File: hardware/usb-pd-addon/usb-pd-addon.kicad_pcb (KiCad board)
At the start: 2 copper layers, 48 x 40 mm, 73 parts, among them J1 Conn_02x10_Odd_Even, J2 Conn_02x10_Odd_Even, J3 USB_TYPE_C, J4 Conn_02x05_Odd_Even, J5 Conn_02x05_Odd_Even, J6 TPAS, J7 TPBS, U1 FUSB302B, U2 AP2171W, U3 SN74AVC1T45DBVR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

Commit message: Updated README, better silk for voltage control jumpers.
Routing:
- net GND: vias 25 -> 28
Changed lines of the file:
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@@
   (general
     (thickness 1.6)
-    (drawings 98)
-    (tracks 589)
+    (drawings 109)
+    (tracks 590)
     (zones 0)
     (modules 73)
@@
     )
   )
+  (gr_poly (pts (xy 56.5785 51.4985) (xy 55.1815 51.4985) (xy 55.1815 50.1015) (xy 56.5785 50.1015)) (layer B.Mask) (width 0.1))
+  (gr_line (start 59.69 36.068) (end 59.69 36.703) (layer F.SilkS) (width 0.12))
+  (gr_line (start 62.23 36.068) (end 62.23 36.703) (layer F.SilkS) (width 0.12))
+  (gr_line (start 64.77 36.068) (end 64.77 36.703) (layer F.SilkS) (width 0.12))
+  (gr_line (start 67.31 36.068) (end 67.31 36.703) (layer F.SilkS) (width 0.12))
+  (gr_line (start 69.85 36.068) (end 69.85 36.703) (layer F.SilkS) (width 0.12))
+  (gr_line (start 52.07 36.068) (end 52.07 36.703) (layer F.SilkS) (width 0.12))
+  (gr_line (start 49.53 36.068) (end 49.53 36.703) (layer F.SilkS) (width 0.12))
+  (gr_line (start 46.99 36.068) (end 46.99 36.703) (layer F.SilkS) (width 0.12))
+  (gr_line (start 44.45 36.068) (end 44.45 36.703) (layer F.SilkS) (width 0.12))
+  (gr_line (start 41.91 36.068) (end 41.91 36.703) (layer F.SilkS) (width 0.12))
   (gr_text 3V3 (at 34.036 66.802 270) (layer F.SilkS)
     (effects (font (size 1 1) (thickness 0.15)))
@@
   (segment (start 76.2 55.88) (end 76.2 58.42) (width 0.3) (layer F.Cu) (net 1) (status 30))
   (segment (start 76.2 58.42) (end 76.2 60.96) (width 0.3) (layer F.Cu) (net 1) (status 30))
-  (via (at 55.88 50.8) (size 0.5) (drill 0.3) (layers F.Cu B.Cu) (net 1) (status 30))
+  (via (at 55.499 50.419) (size 0.5) (drill 0.3) (layers F.Cu B.Cu) (net 1) (status 30))
   (segment (start 59.1312 62.992) (end 59.13 63.552) (width 0.3) (layer F.Cu) (net 1))
   (segment (start 59.13 63.552) (end 59.13 64.535) (width 0.3) (layer F.Cu) (net 1) (status 20))
@@
   (via (at 36.576 66.04) (size 0.5) (drill 0.3) (layers F.Cu B.Cu) (net 1))
   (segment (start 35.56 66.0145) (end 36.5505 66.0145) (width 0.3) (layer F.Cu) (net 1))
+  (via (at 55.499 51.181) (size 0.5) (drill 0.3) (layers F.Cu B.Cu) (net 1) (status 30))
+  (via (at 56.261 51.181) (size 0.5) (drill 0.3) (layers F.Cu B.Cu) (net 1) (status 30))
+  (via (at 56.261 50.419) (size 0.5) (drill 0.3) (layers F.Cu B.Cu) (net 1) (status 30))
   (segment (start 36.83 39.37) (end 38.1 38.1) (width 0.2) (layer F.Cu) (net 4))
   (segment (start 36.83 62.23) (end 36.83 39.37) (width 0.2) (layer F.Cu) (net 4))
@@
   (segment (start 57.1425 52.0625) (end 57.1425 51.3) (width 0.2) (layer F.Cu) (net 7) (status 20))
   (segment (start 56.63 52.0625) (end 57.1425 52.0625) (width 0.2) (layer F.Cu) (net 7) (status 10))
-  (segment (start 57.63 59.535) (end 57.1425 59.0475) (width 0.2) (layer F.Cu) (net 7))
-  (segment (start 57.63 64.535) (end 57.63 59.535) (width 0.2) (layer F.Cu) (net 7) (status 10))
-  (segment (start 57.1425 59.0475) (end 57.1425 53.3475) (width 0.2) (layer F.Cu) (net 7))
   (segment (start 57.1425 53.3475) (end 57.1425 52.0625) (width 0.2) (layer F.Cu) (net 7))
   (segment (start 57.1425 53.3475) (end 57.1425 52.888) (width 0.2) (layer F.Cu) (net 7))
-  (via (at 57.1425 52.888) (size 0.5) (drill 0.3) (layers F.Cu B.Cu) (net 7))
+  (via (at 57.15 60.452) (size 0.5) (drill 0.3) (layers F.Cu B.Cu) (net 7))
+  (segment (start 57.1425 60.8255) (end 57.1425 53.3475) (width 0.2) (layer F.Cu) (net 7))
+  (segment (start 57.63 61.313) (end 57.1425 60.8255) (width 0.2) (layer F.Cu) (net 7))
+  (segment (start 57.63 64.535) (end 57.63 61.313) (width 0.2) (layer F.Cu) (net 7))
   (segment (start 55.118 52.0745) (end 55.13 52.0625) (width 0.2) (layer F.Cu) (net 8) (status 30))
   (segment (start 54.63 64.535) (end 54.58001 64.48501) (width 0.2) (layer F.Cu) (net 8) (status 30))
   (segment (start 54.6175 52.0625) (end 54.6175 51.3) (width 0.2) (layer F.Cu) (net 8) (status 20))
   (segment (start 55.13 52.0625) (end 54.6175 52.0625) (width 0.2) (layer F.Cu) (net 8) (status 10))
-  (segment (start 54.631129 59.085873) (end 54.631129 58.262127) (width 0.2) (layer F.Cu) (net 8))
-  (segment (start 54.525999 59.191003) (end 54.631129 59.085873) (width 0.2) (layer F.Cu) (net 8))
-  (segment (start 54.525999 63.256001) (end 54.525999 59.191003) (width 0.2) (layer F.Cu) (net 8))
-  (segment (start 54.63 63.360002) (end 54.525999 63.256001) (width 0.2) (layer F.Cu) (net 8))
-  (segment (start 54.63 64.535) (end 54.63 63.360002) (width 0.2) (layer F.Cu) (net 8) (status 10))
-  (segment (start 54.631129 58.262127) (end 54.618892 52.696108) (width 0.2) (layer F.Cu) (net 8))
   (segment (start 54.618892 52.696108) (end 54.6175 52.0625) (width 0.2) (layer F.Cu) (net 8))
   (segment (start 54.618892 52.886608) (end 54.618892 52.696108) (width 0.2) (layer F.Cu) (net 8))
-  (via (at 54.618892 52.886608) (size 0.5) (drill 0.3) (layers F.Cu B.Cu) (net 8))
+  (via (at 54.61 60.452) (size 0.5) (drill 0.3) (layers F.Cu B.Cu) (net 8))
+  (segment (start 54.525999 63.256001) (end 54.525999 60.939499) (width 0.2) (layer F.Cu) (net 8))
+  (segment (start 54.618892 60.846606) (end 54.618892 52.696108) (width 0.2) (layer F.Cu) (net 8))
+  (segment (start 54.525999 60.939499) (end 54.618892 60.846606) (width 0.2) (layer F.Cu) (net 8))
+  (segment (start 54.63 63.360002) (end 54.525999 63.256001) (width 0.2) (layer F.Cu) (net 8))
+  (segment (start 54.63 64.535) (end 54.63 63.360002) (width 0.2) (layer F.Cu) (net 8))
   (segment (start 55.13 49.5375) (end 55.13 49.034) (width 0.2) (layer F.Cu) (net 9) (status 10))
   (via (at 54.864 48.768) (size 0.5) (drill 0.3) (layers F.Cu B.Cu) (net 9))
@@
   (segment (start 57.1425 49.7915) (end 57.404 49.53) (width 0.2) (layer F.Cu) (net 14))
   (segment (start 57.1425 50.3) (end 57.1425 49.7915) (width 0.2) (layer F.Cu) (net 14) (status 10))
-  (segment (start 55.8725 51.6965) (end 55.8725 53.3475) (width 0.3) (layer B.Cu) (net 14))
-  (segment (start 57.404 50.165) (end 55.8725 51.6965) (width 0.3) (layer B.Cu) (net 14))
-  (segment (start 57.404 49.53) (end 57.404 50.165) (width 0.3) (layer B.Cu) (net 14))
   (segment (start 64.4525 59.69) (end 62.865 58.1025) (width 0.3) (layer B.Cu) (net 14))
   (segment (start 66.294 59.69) (end 64.4525 59.69) (width 0.3) (layer B.Cu) (net 14))
@@
   (segment (start 69.85 62.23) (end 72.644 65.024) (width 0.3) (layer B.Cu) (net 14))
   (segment (start 66.294 62.23) (end 69.85 62.23) (width 0.3) (layer B.Cu) (net 14))
+  (segment (start 57.404 51.816) (end 55.8725 53.3475) (width 0.3) (layer B.Cu) (net 14))
+  (segment (start 57.404 49.53) (end 57.404 51.816) (width 0.3) (layer B.Cu) (net 14))
   (segment (start 46.0375 48.895) (end 45.085 49.8475) (width 0.3) (layer B.Cu) (net 15))
   (segment (start 52.705 48.895) (end 46.0375 48.895) (width 0.3) (layer B.Cu) (net 15))

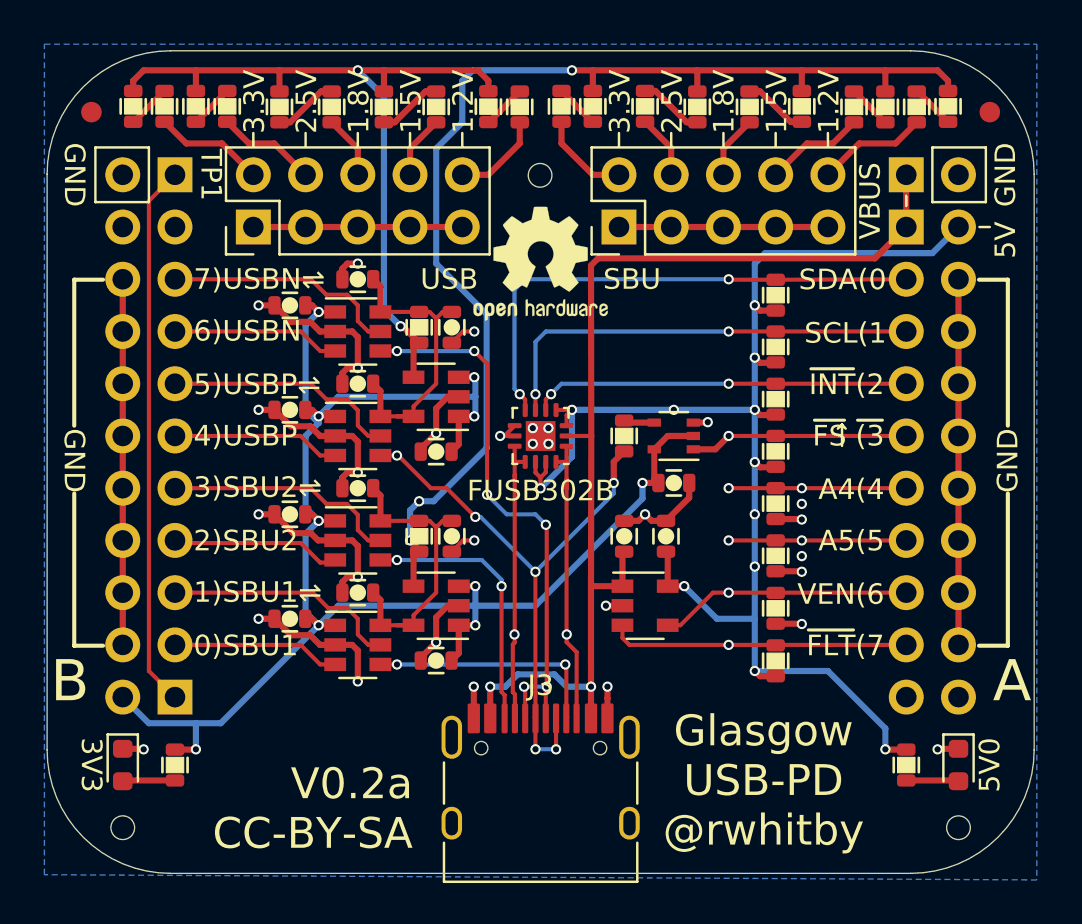
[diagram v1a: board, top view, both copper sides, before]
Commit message: Remove the D+ pullup, cause Glasgow will not support Luna USB stack.  Added 2 spare SOT23 footprints.
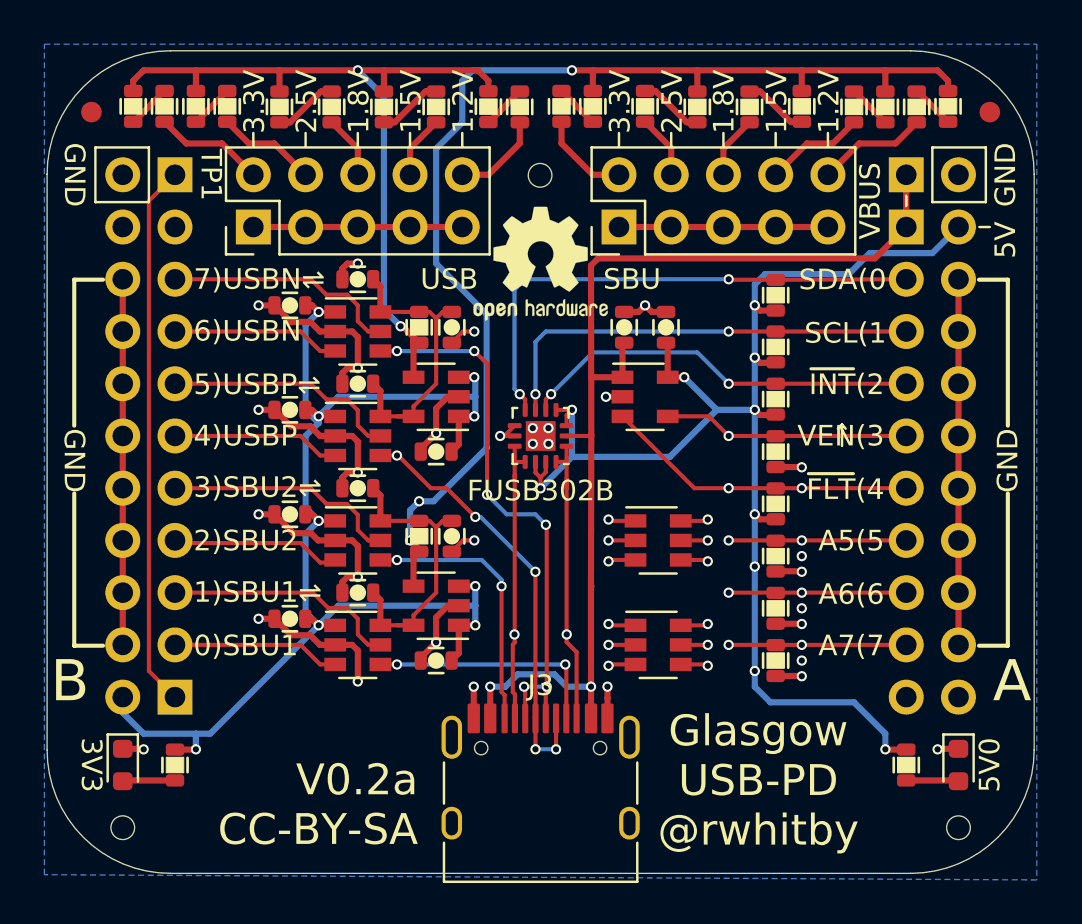
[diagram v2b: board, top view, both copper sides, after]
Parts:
- removed C15: 0.1u, pkl_dipol:C_0603
- removed R31: 1K5, pkl_dipol:R_0603
- removed U9: NC7SZ125P5X, Package_TO_SOT_SMD:SOT-353_SC-70-5
- added J8: Conn_02x03_Odd_Even, Package_TO_SOT_SMD:SOT-23-6, F.Cu at (61.6, 55.9)
- added J9: Conn_02x03_Odd_Even, Package_TO_SOT_SMD:SOT-23-6, F.Cu at (61.6, 61.0)
- moved C13 10.2 mm to (62.0, 45.5)
- moved C14 10.2 mm to (59.9, 45.5)
- moved U2 10.2 mm to (61.0, 48.9)
- moved R8 7.63 mm to (67.3, 54.1)
- moved R7 7.62 mm to (67.3, 51.6)
- moved R4 5.09 mm to (67.3, 56.6)
- moved R5 5.09 mm to (67.3, 59.2)
- moved R6 5.09 mm to (67.3, 61.7)
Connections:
- J2 pad 11: /A4 -> /~FLT
- J2 pad 15: /VEN -> /A6
- J2 pad 17: /~FLT -> /A7
- J2 pad 9: /~FSPU -> /VEN
- R4 pad 1: +5V -> Net-(R4-Pad1)
- R4 pad 2: /~FSPU -> /A5
- R5 pad 2: /A4 -> /A6
- R6 pad 2: /A5 -> /A7
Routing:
- net +3V3: track 80.3 -> 65.0 mm, vias 10 -> 9
- net /~FSPU: track 10.6 -> 0.00 mm, vias 1 -> 0
- net /A7: track 0.00 -> 8.64 mm, vias 0 -> 2
- net /A6: track 0.00 -> 8.64 mm, vias 0 -> 2
- net /A4: track 8.64 -> 0.00 mm, vias 2 -> 0
- net /USBP: track 28.8 -> 21.2 mm, vias 6 -> 5
- net GND: track 113.5 -> 110.5 mm, vias 28 -> 26
- net +5V: track 69.4 -> 67.1 mm, vias 12 -> 10
- net Net-(R31-Pad2): track 1.50 -> 0.00 mm
- net Net-(J9-Pad4): track 0.00 -> 1.34 mm, vias 0 -> 1
- net Net-(J9-Pad3): track 0.00 -> 1.34 mm, vias 0 -> 1
- net Net-(J8-Pad6): track 0.00 -> 1.34 mm, vias 0 -> 1
- net Net-(J8-Pad4): track 0.00 -> 1.34 mm, vias 0 -> 1
- net Net-(J8-Pad3): track 0.00 -> 1.34 mm, vias 0 -> 1
- net Net-(J8-Pad1): track 0.00 -> 1.34 mm, vias 0 -> 1
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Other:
- board text added: "3)VEN"
- board text added: "4)~FLT"
- board text added: "6)A6"
- board text added: "7)A7"
- board text added: "A6(6"
- board text added: "A7(7"
- board text added: "VEN(3"
- board text added: "~FLT~(4"
- board text removed: "3)~FS"
- board text removed: "4)A4"
- board text removed: "6)VEN"
- board text removed: "7)~FLT"
- board text removed: "A4(4"
- board text removed: "VEN(6"
- board text removed: "~FLT~(7"
- board text removed: "~FS ~(3"

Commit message: v0.3a: revamped the level shifting, reusing glasgow hardware for 1.8V to 3.3V
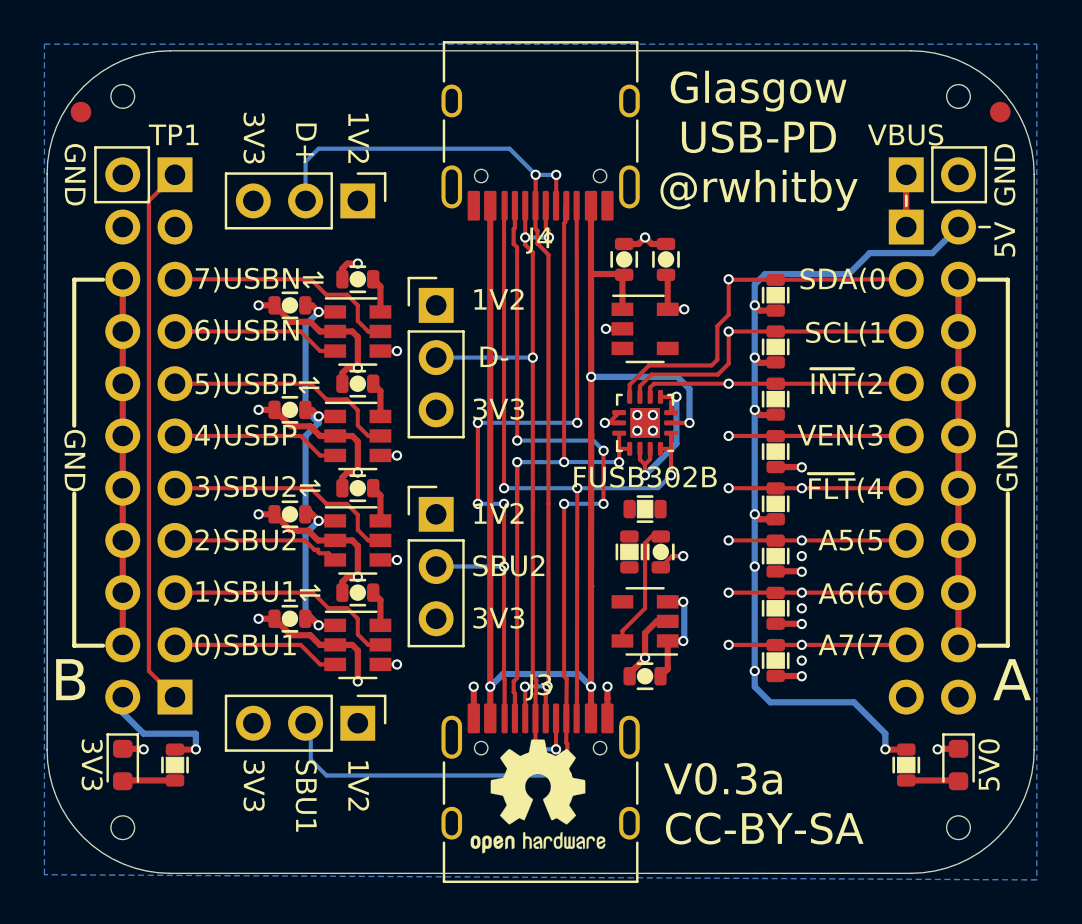
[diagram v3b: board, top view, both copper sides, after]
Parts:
- removed C6, C8: 1uF, pkl_dipol:C_0603
- removed J8, J9: Conn_02x03_Odd_Even, Package_TO_SOT_SMD:SOT-23-6
- removed R10: 10k, pkl_dipol:R_0603
- removed R12, R21: 2K0, pkl_dipol:R_0603
- removed the R13 at (39.1, 34.8)
- removed R14, R23: 4K7, pkl_dipol:R_0603
- removed R15, R22, R26: 1K2, pkl_dipol:R_0603
- removed R16, R25: 6K8, pkl_dipol:R_0603
- removed R17, R28: 1K5, pkl_dipol:R_0603
- removed R18, R27: 10K, pkl_dipol:R_0603
- removed R19, R24, R30: 0R, pkl_dipol:R_0603
- removed R20, R29: 20K, pkl_dipol:R_0603
- removed U8: AP2127K-ADJ, Package_TO_SOT_SMD:SOT-23-5
- added J10: Conn_01x03_Male, Connector_PinHeader_2.54mm:PinHeader_1x03_P2.54mm_Vertical, F.Cu at (50.8, 54.6)
- added J11: Conn_01x03_Male, Connector_PinHeader_2.54mm:PinHeader_1x03_P2.54mm_Vertical, F.Cu at (50.8, 44.5)
- added J12: Conn_01x03_Male, Connector_PinHeader_2.54mm:PinHeader_1x03_P2.54mm_Vertical, F.Cu at (47.0, 64.8)
- added TH4: Mounting_Hole, pkl_pads:ToolingHole, F.Cu at (74.2, 32.3)
- J4: value Conn_02x05_Odd_Even -> USB_TYPE_C; footprint Connector_PinHeader_2.54mm:PinHeader_2x05_P2.54mm_Vertical -> pkl_connectors:USB_C_Receptacle_HRO_TYPE-C-31-M-12
- J5: value Conn_02x05_Odd_Even -> Conn_01x03_Male; footprint Connector_PinHeader_2.54mm:PinHeader_2x05_P2.54mm_Vertical -> Connector_PinHeader_2.54mm:PinHeader_1x03_P2.54mm_Vertical
- R11: value 1K2 -> 20K
- moved R11 32.4 mm to (60.2, 56.4)
- moved LOGO1 25.9 mm to (55.8, 68.3)
- moved LOGO2 25.9 mm to (55.8, 68.3)
- moved TH3 20.7 mm to (33.6, 32.3)
- moved C5 14.9 mm to (61.0, 62.5)
- moved C7 14.9 mm to (61.7, 56.4)
- moved U7 14.9 mm to (61.0, 59.8)
- moved J4 14.9 mm to (55.9, 35.6), turned to 180 degrees
- moved R9 14.1 mm to (61.0, 54.4), turned to 0 degrees
- moved J5 12.8 mm to (47.0, 39.4), turned to 270 degrees
- moved U1 5.12 mm to (61.0, 50.2)
- moved C13 3.30 mm to (62.0, 42.2)
- moved C14 3.30 mm to (59.9, 42.2)
- moved U2 3.30 mm to (61.0, 45.6)
- moved FID1 0.51 mm to (33.5, 35.1)
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- renumbered R32 to R13, R7 to R4, R8 to R5, R4 to R6, R5 to R7, R6 to R8
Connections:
- C11 pad 1: /VIO_USB -> /1.2V
- C12 pad 1: /VIO_SBU -> /1.2V
- C3 pad 1: /VIO_USB -> /1.2V
- C4 pad 1: /VIO_SBU -> /1.2V
- C7 pad 1: /VIO_USB -> /1.2V
- J5 pad 1: GND -> /USBN_1V2
- J5 pad 2: /3V3_SBU -> /USBN
- J5 pad 3: GND -> /USBN_3V3
- R11 pad 1: Net-(R11-Pad1) -> GND
- R9 pad 2: /VIO_USB -> /1.2V
- U3 pad 4: /USBN -> /USBN_1V2
- U3 pad 6: /VIO_USB -> /1.2V
- U4 pad 4: /SBU2 -> /SBU2_1V2
- U4 pad 6: /VIO_SBU -> /1.2V
- U5 pad 4: /USBP -> /USBP_1V2
- U5 pad 6: /VIO_USB -> /1.2V
- U6 pad 4: /SBU1 -> /SBU1_1V2
- U6 pad 6: /VIO_SBU -> /1.2V
- U7 pad 5: /VIO_USB -> /1.2V
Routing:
- net /ADJ_SBU: track 57.0 -> 0.00 mm, vias 3 -> 0
- net /ADJ_USB: track 38.2 -> 0.00 mm, vias 2 -> 0
- net /SBU1: track 11.7 -> 48.3 mm, vias 2 -> 5
- net +3V3: track 65.0 -> 35.4 mm, vias 9 -> 7
- net GND: track 110.5 -> 84.7 mm, vias 26 -> 24
- net /CC2: track 14.4 -> 36.3 mm, vias 1 -> 3
- net /SBU2: track 13.1 -> 34.3 mm, vias 2 -> 5
- net /CC1: track 14.1 -> 34.3 mm, vias 1 -> 3
- net /USBN: track 27.5 -> 45.9 mm, vias 6 -> 4
- net /VBUS: track 52.1 -> 68.7 mm, vias 2 -> 4
- net /USBP: track 21.2 -> 36.9 mm
- net /VIO_USB: track 14.8 -> 0.00 mm
- net /VIO_SBU: track 14.8 -> 0.00 mm
- net /1.2V: track 0.00 -> 13.0 mm
- net +5V: track 67.1 -> 55.0 mm
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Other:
- board text added: "1V2"
- board text added: "D+"
- board text added: "D-"
- board text added: "SBU1"
- board text added: "SBU2"
- board text added: "V0.3a CC-BY-SA"
- board text removed: "1.2V"
- board text removed: "1.5V"
- board text removed: "1.8V"
- board text removed: "2.5V"
- board text removed: "3.3V"
- board text removed: "SBU"
- board text removed: "USB"
- board text removed: "V0.2a CC-BY-SA"
